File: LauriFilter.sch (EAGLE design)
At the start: 27 parts, among them K1 MODE 1, K2 MODE 2

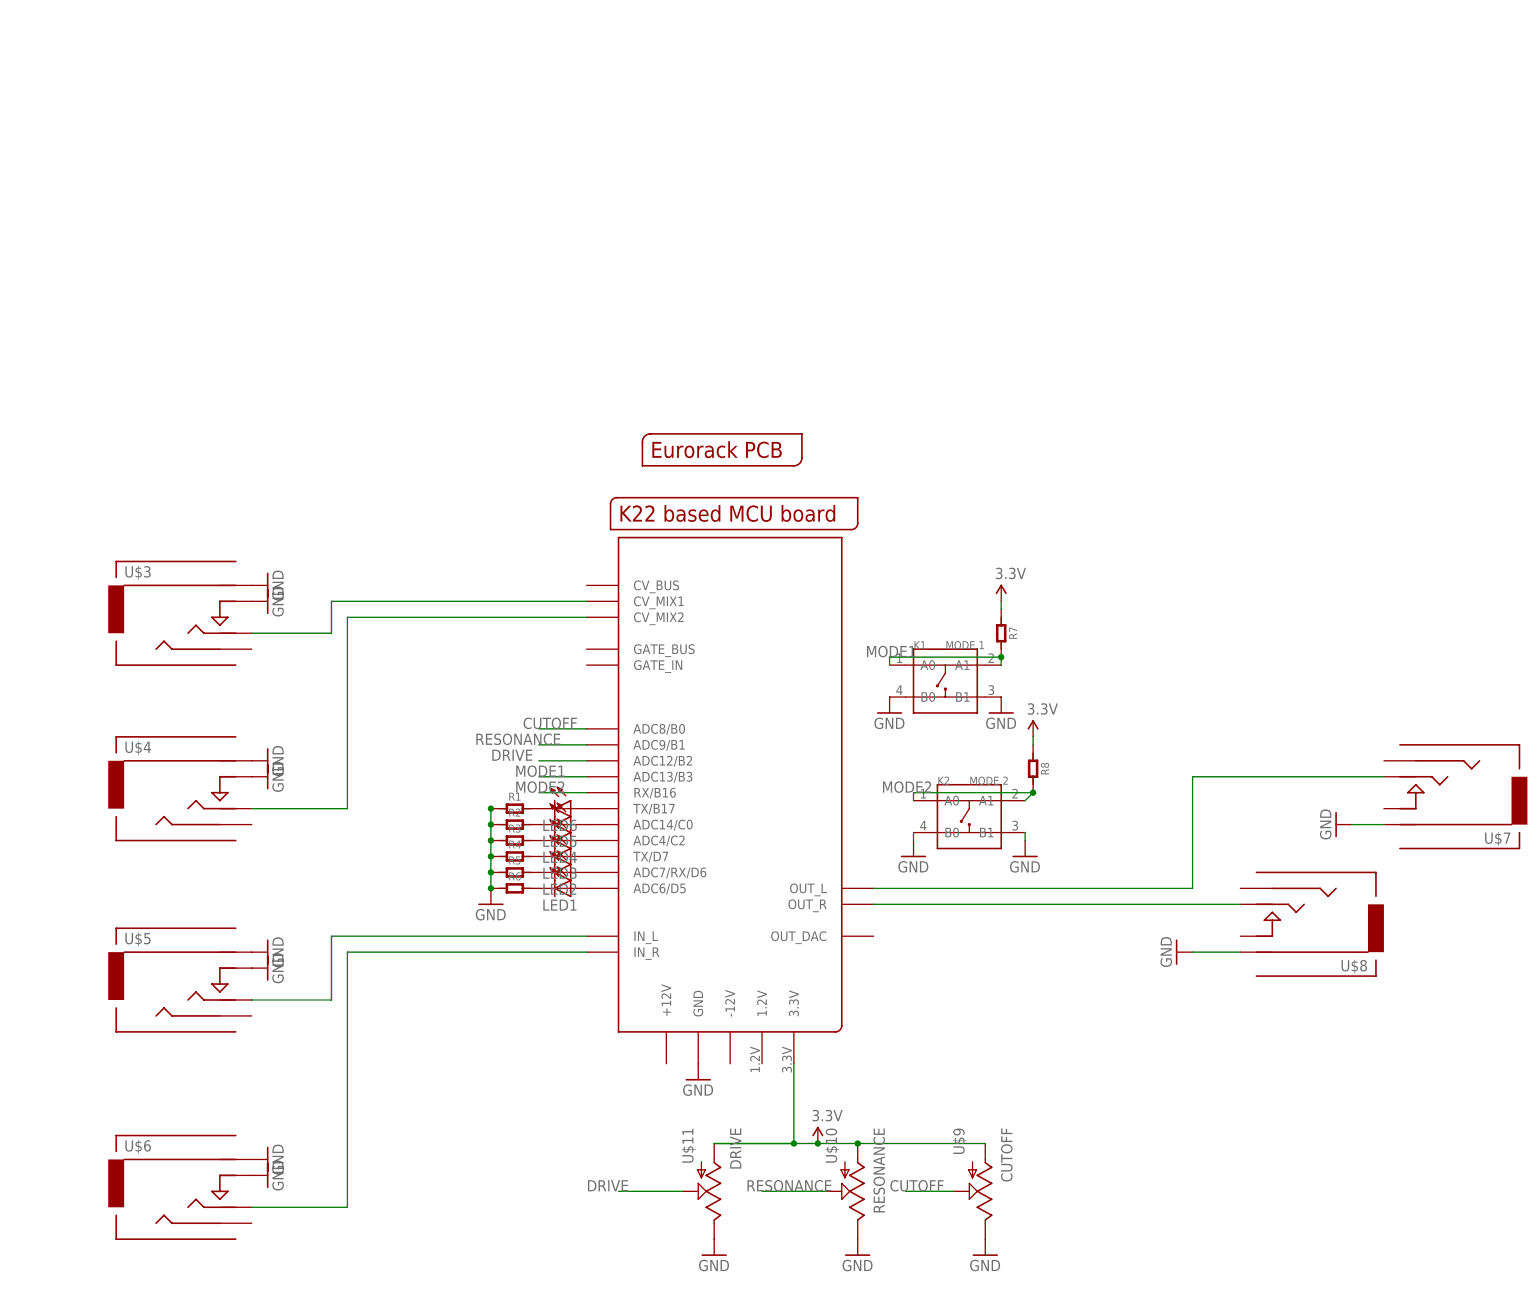
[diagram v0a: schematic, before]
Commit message: LauriFilter has switches + 595 for leds
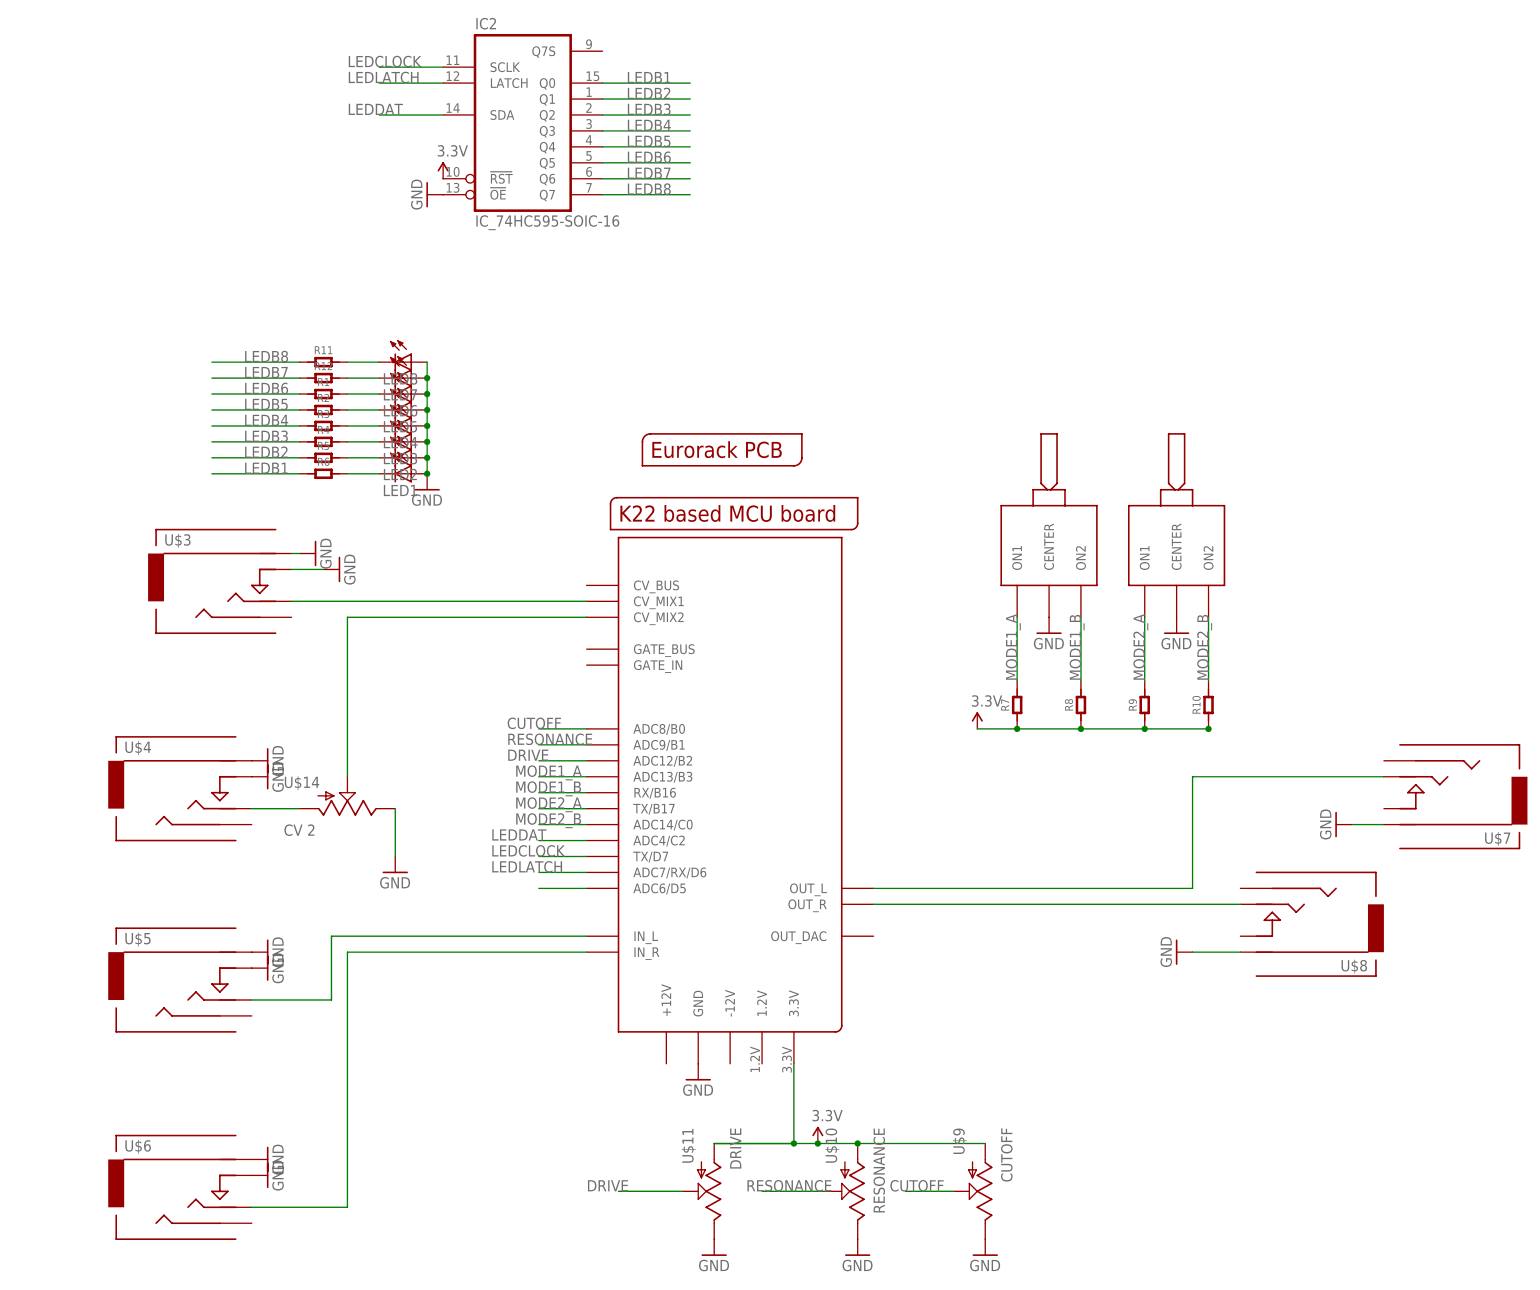
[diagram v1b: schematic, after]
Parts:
- removed K1: MODE 1, OPL:BUTTON-4P-3110040P1
- removed K2: MODE 2, OPL:BUTTON-4P-3110040P1
- added IC2: IC_74HC595-SOIC-16, dp_devices:IC_74HC595-SOIC-16
- added LED7, LED8: (no value), SparkFun-LED:LED3MM
- added R10, R11, R12, R9: (no value), OPL:R-0603
- added U$12, U$13: ONOFFON, EurorackModularParts:ONOFFON
- added U$14: CV 2, EurorackModularParts:POTZEPHPOT
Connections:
- removed net MODE1: K1.A0, K1.A1, R7.2, U$1.ADC13/B3
- removed net MODE2: K2.A0, K2.A1, R8.2, U$1.RX/B16
- removed net N$10: LED3.A, U$1.TX/D7
- removed net N$11: LED4.A, U$1.ADC4/C2
- removed net N$12: LED5.A, U$1.ADC14/C0
- new net LEDB1: IC2IC.Q0
- new net LEDB2: IC2IC.Q1
- new net LEDB3: IC2IC.Q2
- new net LEDB4: IC2IC.Q3
- new net LEDB5: IC2IC.Q4
- new net LEDB6: IC2IC.Q5
- new net LEDB7: IC2IC.Q6
- new net LEDB8: IC2IC.Q7
- new net LEDCLOCK: IC2IC.SCLK, U$1.TX/D7
- new net LEDDAT: IC2IC.SDA, U$1.ADC4/C2
- new net LEDLATCH: IC2IC.LATCH, U$1.ADC7/RX/D6
- new net MODE1_A: R7.2, U$1.ADC13/B3, U$12.ON1
- new net MODE1_B: R8.2, U$1.RX/B16, U$12.ON2
- new net MODE2_A: R9.2, U$1.TX/B17, U$13.ON1
- new net MODE2_B: R10.2, U$1.ADC14/C0, U$13.ON2
- new net N$7: U$14.A, U$4.TIP
- net 3.3V: now also IC2IC.!RST, R10.1, R9.1
- net GND: now also IC2IC.!OE, LED1.A, LED2.A, LED3.A, LED4.A, LED5.A, LED6.A, LED7.A, LED8.A, U$12.CENTER, U$13.CENTER, U$14.E; no longer K1.B0, K1.B1, K2.B0, K2.B1, R1.1, R2.1, R3.1, R4.1, R5.1, R6.1
- net N$13: now also U$1.ADC6/D5; no longer LED6.A, U$1.TX/B17
- net N$4: no longer U$4.TIP
- net N$8: now also LED8.C, R11.2; no longer LED1.A, U$1.ADC6/D5
- net N$9: now also LED7.C, R12.2; no longer LED2.A, U$1.ADC7/RX/D6
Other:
- moved on the sheet: LED1, LED2, LED3, LED4, LED5, LED6, R1, R2, R3, R4, R5, R6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

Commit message: Preliminary routing LauriFilter
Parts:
- added C1: 100nF, OPL:C-0603
- LED1, LED2, LED3, LED4, LED5, LED6, LED7, LED8: value (none) -> WHITE
- R1, R11, R12, R2, R3, R4, R5, R6: value (none) -> 50
- R10, R7, R8, R9: value (none) -> 10k
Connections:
- removed net N$13: U$1.ADC6/D5
- net 3.3V: now also C1.2, IC2SUP.V+, U$1.3.3V
- net GND: now also C1.1, IC2SUP.GND
- net LEDB1: now also R6.1
- net LEDB2: now also R5.1
- net LEDB3: now also R4.1
- net LEDB4: now also R3.1
- net LEDB5: now also R2.1
- net LEDB6: now also R1.1
- net LEDB7: now also R12.1
- net LEDB8: now also R11.1
- net N$4: now also U$14.S
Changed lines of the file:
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@@
 <part name="GND13" library="SparkFun-Aesthetics" deviceset="GND" device=""/>
 <part name="GND14" library="SparkFun-Aesthetics" deviceset="GND" device=""/>
-<part name="LED1" library="SparkFun-LED" deviceset="LED" device="3MM"/>
-<part name="LED2" library="SparkFun-LED" deviceset="LED" device="3MM"/>
-<part name="LED3" library="SparkFun-LED" deviceset="LED" device="3MM"/>
-<part name="LED4" library="SparkFun-LED" deviceset="LED" device="3MM"/>
-<part name="LED5" library="SparkFun-LED" deviceset="LED" device="3MM"/>
-<part name="LED6" library="SparkFun-LED" deviceset="LED" device="3MM"/>
-<part name="R1" library="OPL" deviceset="R*" device="-0603"/>
-<part name="R2" library="OPL" deviceset="R*" device="-0603"/>
-<part name="R3" library="OPL" deviceset="R*" device="-0603"/>
-<part name="R4" library="OPL" deviceset="R*" device="-0603"/>
-<part name="R5" library="OPL" deviceset="R*" device="-0603"/>
-<part name="R6" library="OPL" deviceset="R*" device="-0603"/>
+<part name="LED1" library="SparkFun-LED" deviceset="LED" device="3MM" value="WHITE"/>
+<part name="LED2" library="SparkFun-LED" deviceset="LED" device="3MM" value="WHITE"/>
+<part name="LED3" library="SparkFun-LED" deviceset="LED" device="3MM" value="WHITE"/>
+<part name="LED4" library="SparkFun-LED" deviceset="LED" device="3MM" value="WHITE"/>
+<part name="LED5" library="SparkFun-LED" deviceset="LED" device="3MM" value="WHITE"/>
+<part name="LED6" library="SparkFun-LED" deviceset="LED" device="3MM" value="WHITE"/>
+<part name="R1" library="OPL" deviceset="R*" device="-0603" value="50"/>
+<part name="R2" library="OPL" deviceset="R*" device="-0603" value="50"/>
+<part name="R3" library="OPL" deviceset="R*" device="-0603" value="50"/>
+<part name="R4" library="OPL" deviceset="R*" device="-0603" value="50"/>
+<part name="R5" library="OPL" deviceset="R*" device="-0603" value="50"/>
+<part name="R6" library="OPL" deviceset="R*" device="-0603" value="50"/>
 <part name="SUPPLY3" library="SparkFun-Aesthetics" deviceset="3.3V" device=""/>
 <part name="U$12" library="EurorackModularParts" deviceset="ONOFFON" device=""/>
@@
 <part name="GND17" library="SparkFun-Aesthetics" deviceset="GND" device=""/>
 <part name="GND18" library="SparkFun-Aesthetics" deviceset="GND" device=""/>
-<part name="R7" library="OPL" deviceset="R*" device="-0603"/>
-<part name="R8" library="OPL" deviceset="R*" device="-0603"/>
-<part name="R9" library="OPL" deviceset="R*" device="-0603"/>
-<part name="R10" library="OPL" deviceset="R*" device="-0603"/>
+<part name="R7" library="OPL" deviceset="R*" device="-0603" value="10k"/>
+<part name="R8" library="OPL" deviceset="R*" device="-0603" value="10k"/>
+<part name="R9" library="OPL" deviceset="R*" device="-0603" value="10k"/>
+<part name="R10" library="OPL" deviceset="R*" device="-0603" value="10k"/>
 <part name="SUPPLY1" library="SparkFun-Aesthetics" deviceset="3.3V" device=""/>
-<part name="LED7" library="SparkFun-LED" deviceset="LED" device="3MM"/>
-<part name="LED8" library="SparkFun-LED" deviceset="LED" device="3MM"/>
-<part name="R11" library="OPL" deviceset="R*" device="-0603"/>
-<part name="R12" library="OPL" deviceset="R*" device="-0603"/>
+<part name="LED7" library="SparkFun-LED" deviceset="LED" device="3MM" value="WHITE"/>
+<part name="LED8" library="SparkFun-LED" deviceset="LED" device="3MM" value="WHITE"/>
+<part name="R11" library="OPL" deviceset="R*" device="-0603" value="50"/>
+<part name="R12" library="OPL" deviceset="R*" device="-0603" value="50"/>
 <part name="IC2" library="dp_devices" deviceset="IC_74HC595" device="-SOIC-16"/>
 <part name="GND20" library="SparkFun" deviceset="GND" device=""/>
 <part name="SUPPLY4" library="SparkFun-Aesthetics" deviceset="3.3V" device=""/>
 <part name="GND15" library="SparkFun-Aesthetics" deviceset="GND" device=""/>
+<part name="C1" library="OPL" deviceset="C*" device="-0603" value="100nF"/>
+<part name="GND19" library="SparkFun" deviceset="GND" device=""/>
+<part name="GND21" library="SparkFun" deviceset="GND" device=""/>
+<part name="SUPPLY2" library="SparkFun-Aesthetics" deviceset="3.3V" device=""/>
+<part name="SUPPLY5" library="SparkFun-Aesthetics" deviceset="3.3V" device=""/>
 </parts>
 <sheets>
@@
 <instance part="SUPPLY4" gate="G$1" x="-5.08" y="135.89"/>
 <instance part="GND15" gate="1" x="-7.62" y="86.36"/>
+<instance part="C1" gate="C" x="-35.56" y="129.54" rot="R90"/>
+<instance part="IC2" gate="SUP" x="-27.94" y="129.54"/>
+<instance part="GND19" gate="1" x="-35.56" y="123.19"/>
+<instance part="GND21" gate="1" x="-27.94" y="114.3"/>
+<instance part="SUPPLY2" gate="G$1" x="-27.94" y="142.24"/>
+<instance part="SUPPLY5" gate="G$1" x="-35.56" y="133.35"/>
 </instances>
 <busses>
@@
 <junction x="-7.62" y="104.14"/>
 </segment>
+<segment>
+<pinref part="C1" gate="C" pin="1"/>
+<pinref part="GND19" gate="1" pin="GND"/>
+</segment>
+<segment>
+<pinref part="IC2" gate="SUP" pin="GND"/>
+<pinref part="GND21" gate="1" pin="GND"/>
+</segment>
 </net>
 <net name="N$1" class="0">
@@
 <wire x1="17.78" y1="66.04" x2="-20.32" y2="66.04" width="0.1524" layer="91"/>
 <wire x1="-20.32" y1="66.04" x2="-20.32" y2="40.64" width="0.1524" layer="91"/>
+<pinref part="U$14" gate="G$1" pin="S"/>
+<junction x="-20.32" y="40.64"/>
 </segment>
 </net>
@@
 <pinref part="SUPPLY3" gate="G$1" pin="3.3V"/>
 <junction x="54.61" y="-17.78"/>
+<junction x="38.1" y="-17.78"/>
+<pinref part="U$1" gate="G$1" pin="3.3V"/>
+<junction x="50.8" y="-5.08"/>
 </segment>
 <segment>
@@
 <pinref part="SUPPLY4" gate="G$1" pin="3.3V"/>
 </segment>
+<segment>
+<pinref part="IC2" gate="SUP" pin="V+"/>
+<pinref part="SUPPLY2" gate="G$1" pin="3.3V"/>
+</segment>
+<segment>
+<pinref part="C1" gate="C" pin="2"/>
+<pinref part="SUPPLY5" gate="G$1" pin="3.3V"/>
+</segment>
 </net>
 <net name="MODE1_A" class="0">
@@
 </segment>
 </net>
-<net name="N$13" class="0">
-<segment>
-<pinref part="U$1" gate="G$1" pin="ADC6/D5"/>
-<wire x1="17.78" y1="22.86" x2="10.16" y2="22.86" width="0.1524" layer="91"/>
-</segment>
-</net>
 <net name="N$8" class="0">
 <segment>
@@
 <wire x1="-41.91" y1="88.9" x2="-27.94" y2="88.9" width="0.1524" layer="91"/>
 <label x="-36.83" y="88.9" size="1.778" layer="95"/>
+<pinref part="R6" gate="R" pin="1"/>
+<junction x="-27.94" y="88.9"/>
 </segment>
 </net>
@@
 <wire x1="-41.91" y1="91.44" x2="-27.94" y2="91.44" width="0.1524" layer="91"/>
 <label x="-36.83" y="91.44" size="1.778" layer="95"/>
+<pinref part="R5" gate="R" pin="1"/>
+<junction x="-27.94" y="91.44"/>
 </segment>
 </net>
@@
 <wire x1="-41.91" y1="93.98" x2="-27.94" y2="93.98" width="0.1524" layer="91"/>
 <label x="-36.83" y="93.98" size="1.778" layer="95"/>
+<pinref part="R4" gate="R" pin="1"/>
+<junction x="-27.94" y="93.98"/>
 </segment>
 </net>
@@
 <wire x1="-41.91" y1="96.52" x2="-27.94" y2="96.52" width="0.1524" layer="91"/>
 <label x="-36.83" y="96.52" size="1.778" layer="95"/>
+<pinref part="R3" gate="R" pin="1"/>
+<junction x="-27.94" y="96.52"/>
 </segment>
 </net>
@@
 <wire x1="-41.91" y1="99.06" x2="-27.94" y2="99.06" width="0.1524" layer="91"/>
 <label x="-36.83" y="99.06" size="1.778" layer="95"/>
+<pinref part="R2" gate="R" pin="1"/>
+<junction x="-27.94" y="99.06"/>
 </segment>
 </net>
@@
 <wire x1="-41.91" y1="101.6" x2="-27.94" y2="101.6" width="0.1524" layer="91"/>
 <label x="-36.83" y="101.6" size="1.778" layer="95"/>
+<pinref part="R1" gate="R" pin="1"/>
+<junction x="-27.94" y="101.6"/>
 </segment>
 </net>
@@
 <wire x1="-41.91" y1="104.14" x2="-27.94" y2="104.14" width="0.1524" layer="91"/>
 <label x="-36.83" y="104.14" size="1.778" layer="95"/>
+<pinref part="R12" gate="R" pin="1"/>
+<junction x="-27.94" y="104.14"/>
 </segment>
 </net>
@@
 <wire x1="-41.91" y1="106.68" x2="-27.94" y2="106.68" width="0.1524" layer="91"/>
 <label x="-36.83" y="106.68" size="1.778" layer="95"/>
+<pinref part="R11" gate="R" pin="1"/>
+<junction x="-27.94" y="106.68"/>
 </segment>
 </net>
@@
 </sheet>
 </sheets>
+<errors>
+</errors>
 </schematic>
 </drawing>

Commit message: Many many changes after crosschecking by Lauri
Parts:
- added R13: 100k, OPL:R-0603
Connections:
- new net N$10: R13.2, U$14.A
- net N$7: now also R13.1; no longer U$14.A
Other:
- moved on the sheet: U$4
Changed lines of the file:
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@@
 <setting verticaltext="up"/>
 </settings>
-<grid distance="0.05" unitdist="inch" unit="inch" style="lines" multiple="1" display="no" altdistance="0.01" altunitdist="inch" altunit="inch"/>
+<grid distance="0.1" unitdist="inch" unit="inch" style="lines" multiple="1" display="no" altdistance="0.01" altunitdist="inch" altunit="inch"/>
 <layers>
 <layer number="1" name="Top" color="4" fill="1" visible="no" active="no"/>
@@
 <part name="SUPPLY2" library="SparkFun-Aesthetics" deviceset="3.3V" device=""/>
 <part name="SUPPLY5" library="SparkFun-Aesthetics" deviceset="3.3V" device=""/>
+<part name="R13" library="OPL" deviceset="R*" device="-0603" value="100k"/>
 </parts>
 <sheets>
@@
 <instance part="U$2" gate="G$1" x="27.94" y="91.44"/>
 <instance part="U$3" gate="G$1" x="-36.83" y="73.66"/>
-<instance part="U$4" gate="G$1" x="-43.18" y="40.64"/>
+<instance part="U$4" gate="G$1" x="-58.42" y="40.64"/>
 <instance part="U$5" gate="G$1" x="-43.18" y="10.16"/>
 <instance part="U$6" gate="G$1" x="-43.18" y="-22.86"/>
@@
 <instance part="SUPPLY2" gate="G$1" x="-27.94" y="142.24"/>
 <instance part="SUPPLY5" gate="G$1" x="-35.56" y="133.35"/>
+<instance part="R13" gate="R" x="-39.37" y="35.56"/>
 </instances>
 <busses>
@@
 <pinref part="U$4" gate="G$1" pin="SWITCH"/>
 <pinref part="GND3" gate="1" pin="GND"/>
+<wire x1="-50.8" y1="40.64" x2="-35.56" y2="40.64" width="0.1524" layer="91"/>
 </segment>
 <segment>
 <pinref part="U$4" gate="G$1" pin="RING"/>
 <pinref part="GND4" gate="1" pin="GND"/>
+<wire x1="-50.8" y1="43.18" x2="-35.56" y2="43.18" width="0.1524" layer="91"/>
 </segment>
 <segment>
@@
 <segment>
 <pinref part="U$4" gate="G$1" pin="TIP"/>
-<pinref part="U$14" gate="G$1" pin="A"/>
-<wire x1="-27.94" y1="35.56" x2="-35.56" y2="35.56" width="0.1524" layer="91"/>
+<pinref part="R13" gate="R" pin="1"/>
+<wire x1="-43.18" y1="35.56" x2="-50.8" y2="35.56" width="0.1524" layer="91"/>
 </segment>
 </net>
@@
 </segment>
 </net>
+<net name="N$10" class="0">
+<segment>
+<pinref part="U$14" gate="G$1" pin="A"/>
+<wire x1="-27.94" y1="35.56" x2="-35.56" y2="35.56" width="0.1524" layer="91"/>
+<pinref part="R13" gate="R" pin="2"/>
+</segment>
+</net>
